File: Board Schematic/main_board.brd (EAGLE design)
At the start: 58.4 x 108.9 mm, 16 parts, among them J1 RJ11, J2 COMP, J3 INT_PROBE, J4 RHT03, J5 D_C_SELECT, J6 EXT_PROBE, J7 COND_FAN, J8 EVAP_FAN, J9 AC_IN, K1 RELAY-SPDT-JQX-15F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

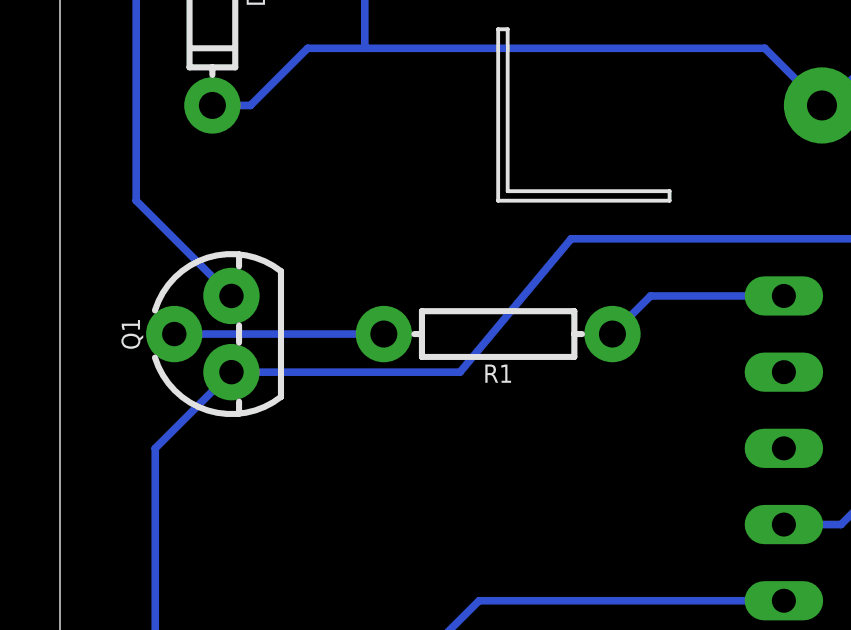
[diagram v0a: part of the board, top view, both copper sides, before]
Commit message: Fixed a trace clearance issue
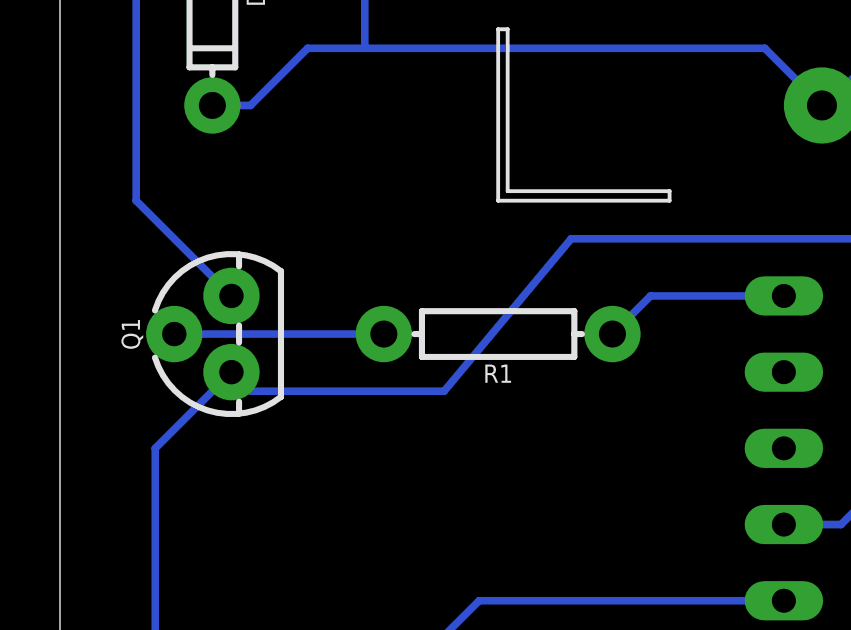
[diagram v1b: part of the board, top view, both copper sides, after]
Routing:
- net GND: track 147.5 -> 148.0 mm
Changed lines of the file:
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@@
 <?xml version="1.0" encoding="utf-8"?>
 <!DOCTYPE eagle SYSTEM "eagle.dtd">
-<eagle version="9.3.0">
+<eagle version="9.3.1">
 <drawing>
 <settings>
@@
 <wire x1="50.8" y1="25.4" x2="46.99" y2="21.59" width="0.254" layer="16"/>
 <wire x1="5.7912" y1="36.8808" x2="5.715" y2="36.83" width="0.1524" layer="16"/>
-<wire x1="5.715" y1="36.83" x2="13.335" y2="36.83" width="0.254" layer="16"/>
-<wire x1="13.335" y1="36.83" x2="17.039165625" y2="41.275" width="0.254" layer="16"/>
+<wire x1="12.805834375" y1="36.195" x2="6.35" y2="36.195" width="0.254" layer="16"/>
+<wire x1="5.715" y1="36.83" x2="6.35" y2="36.195" width="0.254" layer="16"/>
+<wire x1="12.805834375" y1="36.195" x2="17.039165625" y2="41.275" width="0.254" layer="16"/>
 <wire x1="17.039165625" y1="41.275" x2="29.68625" y2="41.275" width="0.254" layer="16"/>
 <wire x1="29.68625" y1="41.275" x2="33.02" y2="45.72" width="0.254" layer="16"/>

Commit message: Cleanup and BOM addition
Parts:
- moved R1 10.0 mm to (6.35, 32.4)
- moved Q1 3.81 mm to (9.53, 38.1)
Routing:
- net RELAY_EN: track 6.24 -> 16.9 mm
- net N$2: track 55.1 -> 57.7 mm
- net GND: track 148.0 -> 145.5 mm
- net 5V: track 194.3 -> 195.6 mm
- net N$1: track 6.98 -> 7.82 mm
- net EXT_A: track 28.6 -> 29.2 mm
